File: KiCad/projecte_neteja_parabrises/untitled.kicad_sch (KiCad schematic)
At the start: 14 parts, among them J2 DE9_Pins, J3 DE9_Pins, SW1 CALEFACTOR, SW2 BOMBAS, SW5 SW_Rotary_1x5_MP, U1 TJA1049TK-3, U7 MAX232

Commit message: Error de nombres solucionado
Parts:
- renumbered U1 to U8, U7 to U9
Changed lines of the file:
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@@
 		(dnp no)
 		(fields_autoplaced yes)
-		(property "Reference" "U7"
+		(property "Reference" "U9"
 			(at 56.7533 31.75 0)
 			(effects
@@
 			(project "projecte_neteja_parabrises"
 				(path "/83fe8808-b70b-463e-9fcd-89556c9690a9/281f4b1b-fa83-45a0-8e9c-797a6b6648f6"
-					(reference "U7")
+					(reference "U9")
 					(unit 1)
 				)
@@
 		(dnp no)
 		(fields_autoplaced yes)
-		(property "Reference" "U1"
+		(property "Reference" "U8"
 			(at 209.7883 54.61 0)
 			(effects
@@
 			(project "projecte_neteja_parabrises"
 				(path "/83fe8808-b70b-463e-9fcd-89556c9690a9/281f4b1b-fa83-45a0-8e9c-797a6b6648f6"
-					(reference "U1")
-					(unit 1)
-				)
+					(reference "U8")
+					(unit 1)
+				)

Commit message: huellas
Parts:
- C18, C19, C5, C6, C7, C8, C9: footprint (none) -> Capacitor_SMD:C_0805_2012Metric
- U9: footprint (none) -> Package_SO:JEITA_SOIC-16_3.9x9.9mm_P1.27mm
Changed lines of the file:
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@@
 			)
 		)
-		(property "Footprint" ""
+		(property "Footprint" "Capacitor_SMD:C_0805_2012Metric"
 			(at 78.105 53.0352 0)
 			(effects
@@
 			)
 		)
-		(property "Footprint" ""
+		(property "Footprint" "Capacitor_SMD:C_0805_2012Metric"
 			(at 230.2002 68.58 0)
 			(effects
@@
 			)
 		)
-		(property "Footprint" ""
+		(property "Footprint" "Package_SO:JEITA_SOIC-16_3.9x9.9mm_P1.27mm"
 			(at 55.88 88.9 0)
 			(effects
@@
 			)
 		)
-		(property "Footprint" ""
+		(property "Footprint" "Capacitor_SMD:C_0805_2012Metric"
 			(at 78.4352 46.99 0)
 			(effects
@@
 			)
 		)
-		(property "Footprint" ""
+		(property "Footprint" "Capacitor_SMD:C_0805_2012Metric"
 			(at 30.1752 46.99 0)
 			(effects
@@
 			)
 		)
-		(property "Footprint" ""
+		(property "Footprint" "Capacitor_SMD:C_0805_2012Metric"
 			(at 79.375 60.6552 0)
 			(effects
@@
 			)
 		)
-		(property "Footprint" ""
+		(property "Footprint" "Capacitor_SMD:C_0805_2012Metric"
 			(at 230.2002 76.2 0)
 			(effects
@@
 			)
 		)
-		(property "Footprint" ""
+		(property "Footprint" "Capacitor_SMD:C_0805_2012Metric"
 			(at 54.61 25.7048 0)
 			(effects

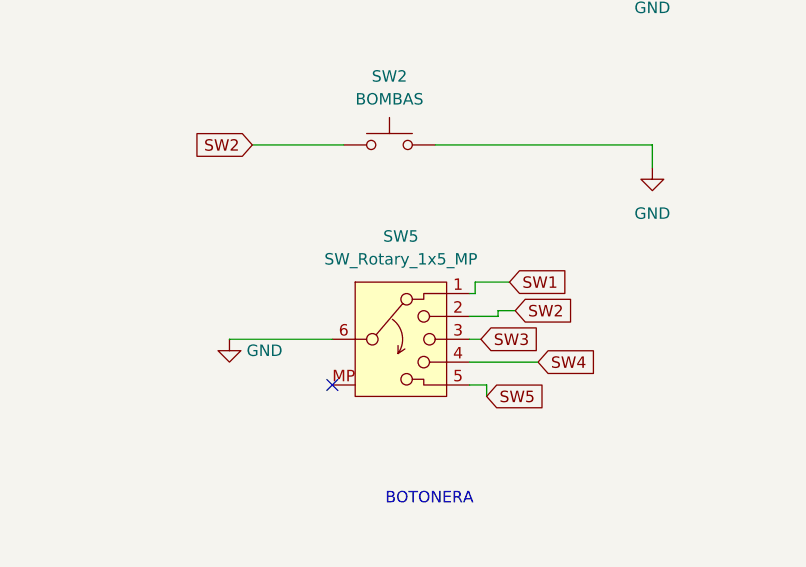
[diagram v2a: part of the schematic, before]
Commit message: Actualización huellas
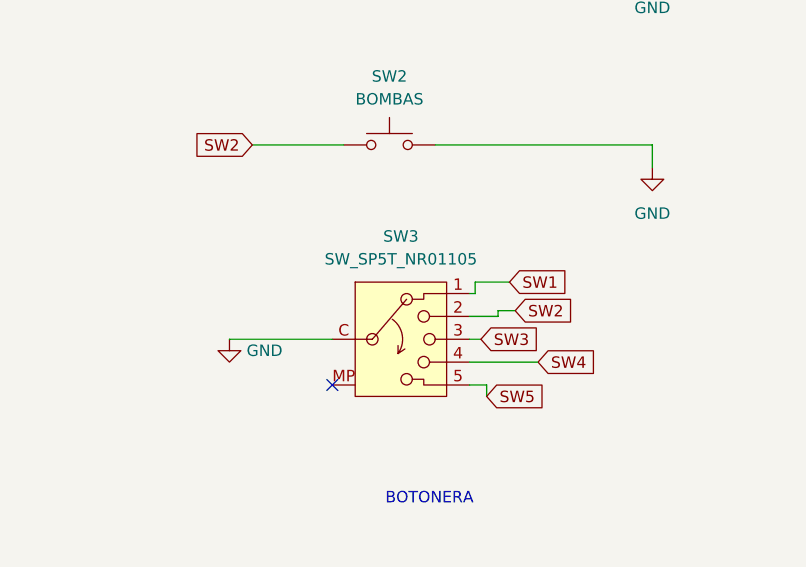
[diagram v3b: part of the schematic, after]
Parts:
- removed SW5: SW_Rotary_1x5_MP, symbol Switch:SW_Rotary_1x5_MP
- added SW3: SW_SP5T_NR01105, Button_Switch_THT:SW_NKK_NR01, symbol Switch:SW_SP5T_NR01105
- J2, J3: footprint (none) -> Connector_Dsub:DSUB-9_Pins_Horizontal_P2.77x2.84mm_EdgePinOffset4.94mm_Housed_MountingHolesOffset4.94mm
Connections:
- net GND: now also SW3.C (Common)
- net SW1: now also SW3.1
- net SW2: now also SW3.2
- net SW3: now also SW3.3
- net SW4: now also SW3.4
- net SW5: now also SW3.5
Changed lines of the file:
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@@
 			)
 		)
-		(property "Footprint" ""
+		(property "Footprint" "Connector_Dsub:DSUB-9_Pins_Horizontal_P2.77x2.84mm_EdgePinOffset4.94mm_Housed_MountingHolesOffset4.94mm"
 			(at 254.635 66.675 0)
 			(effects
@@
 			)
 		)
-		(property "Footprint" ""
+		(property "Footprint" "Connector_Dsub:DSUB-9_Pins_Horizontal_P2.77x2.84mm_EdgePinOffset4.94mm_Housed_MountingHolesOffset4.94mm"
 			(at 111.125 71.12 0)
 			(effects
@@
 	)
 	(symbol
+		(lib_id "Switch:SW_SP5T_NR01105")
+		(at 54.61 173.99 0)
+		(unit 1)
+		(exclude_from_sim no)
+		(in_bom yes)
+		(on_board yes)
+		(dnp no)
+		(fields_autoplaced yes)
+		(property "Reference" "SW3"
+			(at 54.61 162.56 0)
+			(effects
+				(font
+					(size 1.27 1.27)
+				)
+			)
+		)
+		(property "Value" "SW_SP5T_NR01105"
+			(at 54.61 165.1 0)
+			(effects
+				(font
+					(size 1.27 1.27)
+				)
+			)
+		)
+		(property "Footprint" "Button_Switch_THT:SW_NKK_NR01"
+			(at 54.61 184.15 0)
+			(effects
+				(font
+					(size 1.27 1.27)
+				)
+				(hide yes)
+			)
+		)
+		(property "Datasheet" "https://www.nkkswitches.com/pdf/NR01%20Rotaries.pdf"
+			(at 54.61 186.69 0)
+			(effects
+				(font
+					(size 1.27 1.27)
+				)
+				(hide yes)
+			)
+		)
+		(property "Description" "NKK Switches NR01 Series rotary SP5T switch"
+			(at 54.61 173.99 0)
+			(effects
+				(font
+					(size 1.27 1.27)
+				)
+				(hide yes)
+			)
+		)
+		(pin "C"
+		)
+		(pin "1"
+		)
+		(pin "2"
+		)
+		(pin "MP"
+		)
+		(pin "4"
+		)
+		(pin "3"
+		)
+		(pin "5"
+		)
+		(instances
+			(project ""
+				(path "/83fe8808-b70b-463e-9fcd-89556c9690a9/281f4b1b-fa83-45a0-8e9c-797a6b6648f6"
+					(reference "SW3")
+					(unit 1)
+				)
+			)
+		)
+	)
+	(symbol
 		(lib_id "power:GND")
 		(at 85.725 52.07 0)
@@
 					(unit 1)
 				)
-			)
-		)
-	)
-	(symbol
-		(lib_id "Switch:SW_Rotary_1x5_MP")
-		(at 54.61 173.99 0)
-		(unit 1)
-		(exclude_from_sim no)
-		(in_bom yes)
-		(on_board yes)
-		(dnp no)
-		(fields_autoplaced yes)
-		(property "Reference" "SW5"
-			(at 54.61 162.56 0)
-			(effects
-				(font
-					(size 1.27 1.27)
-				)
-			)
-		)
-		(property "Value" "SW_Rotary_1x5_MP"
-			(at 54.61 165.1 0)
-			(effects
-				(font
-					(size 1.27 1.27)
-				)
-			)
-		)
-		(property "Footprint" ""
-			(at 54.61 184.15 0)
-			(effects
-				(font
-					(size 1.27 1.27)
-				)
-				(hide yes)
-			)
-		)
-		(property "Datasheet" "~"
-			(at 54.61 186.69 0)
-			(effects
-				(font
-					(size 1.27 1.27)
-				)
-				(hide yes)
-			)
-		)
-		(property "Description" "Rotary switch 1x5, SP5T with mount point"
-			(at 54.61 173.99 0)
-			(effects
-				(font
-					(size 1.27 1.27)
-				)
-				(hide yes)
-			)
-		)
-		(pin "1"
-		)
-		(pin "2"
-		)
-		(pin "MP"
-		)
-		(pin "3"
-		)
-		(pin "4"
-		)
-		(pin "6"
-		)
-		(pin "5"
-		)
-		(instances
-			(project "projecte_neteja_parabrises"
-				(path "/83fe8808-b70b-463e-9fcd-89556c9690a9/281f4b1b-fa83-45a0-8e9c-797a6b6648f6"
-					(reference "SW5")
-					(unit 1)
-				)

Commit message: botonera
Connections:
- net SW1: no longer SW1.1
- net SW2: no longer SW2.1
- new net SWB: SW2.1
- new net SWC: SW1.1
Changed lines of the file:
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@@
 		)
 	)
-	(global_label "SW2"
+	(global_label "SWB"
 		(shape input)
 		(at 38.1 152.4 180)
@@
 		)
 		(property "Intersheetrefs" "${INTERSHEET_REFS}"
-			(at 31.2444 152.4 0)
+			(at 31.1839 152.4 0)
 			(effects
 				(font
@@
 		)
 	)
-	(global_label "SW1"
+	(global_label "SWC"
 		(shape input)
 		(at 38.1 129.54 180)
@@
 		)
 		(property "Intersheetrefs" "${INTERSHEET_REFS}"
-			(at 31.2444 129.54 0)
+			(at 31.1839 129.54 0)
 			(effects
 				(font

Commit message: Placa definitiva
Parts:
- J2, J3: footprint Connector_Dsub:DSUB-9_Pins_Horizontal_P2.77x2.84mm_EdgePinOffset4.94mm_Housed_MountingHolesOffset4.94mm -> Connector_Dsub:DSUB-9_Pins_Vertical_P2.77x2.84mm
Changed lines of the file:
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@@
-	(wire
-		(pts
-			(xy 65.405 170.815) (xy 65.405 171.45)
-		)
-		(stroke
-			(width 0)
-			(type default)
-		)
-	)
 	(wire
 		(pts
@@
 	(wire
 		(pts
-			(xy 62.865 167.64) (xy 62.865 168.91)
-		)
-		(stroke
-			(width 0)
-			(type default)
-		)
-	)
-	(wire
-		(pts
 			(xy 76.835 74.93) (xy 74.93 74.93)
 		)
@@
 	(wire
 		(pts
-			(xy 64.135 179.07) (xy 62.23 179.07)
+			(xy 65.405 179.07) (xy 62.23 179.07)
 		)
 		(stroke
@@
 	(wire
 		(pts
-			(xy 62.865 168.91) (xy 62.23 168.91)
+			(xy 62.23 168.91) (xy 69.215 168.91)
 		)
 		(stroke
@@
 	(wire
 		(pts
-			(xy 64.135 180.34) (xy 64.135 179.07)
-		)
-		(stroke
-			(width 0)
-			(type default)
-		)
-	)
-	(wire
-		(pts
-			(xy 67.31 170.815) (xy 65.405 170.815)
-		)
-		(stroke
-			(width 0)
-			(type default)
-		)
-	)
-	(wire
-		(pts
 			(xy 229.235 68.58) (xy 238.125 68.58)
 		)
@@
 	(wire
 		(pts
-			(xy 62.865 167.64) (xy 66.675 167.64)
-		)
-		(stroke
-			(width 0)
-			(type default)
-		)
-	)
-	(wire
-		(pts
 			(xy 220.345 60.96) (xy 220.345 64.77)
 		)
@@
 	(wire
 		(pts
-			(xy 69.85 176.53) (xy 62.23 176.53)
+			(xy 76.2 176.53) (xy 62.23 176.53)
 		)
 		(stroke
@@
 	(wire
 		(pts
-			(xy 65.405 171.45) (xy 62.23 171.45)
+			(xy 62.23 171.45) (xy 75.565 171.45)
 		)
 		(stroke
@@
 	(global_label "SW2"
 		(shape input)
-		(at 67.31 170.815 0)
+		(at 75.565 171.45 0)
 		(fields_autoplaced yes)
 		(effects
@@
 		)
 		(property "Intersheetrefs" "${INTERSHEET_REFS}"
-			(at 74.1656 170.815 0)
+			(at 82.4206 171.45 0)
 			(effects
 				(font
@@
 	(global_label "SW5"
 		(shape input)
-		(at 64.135 180.34 0)
+		(at 65.405 179.07 0)
 		(fields_autoplaced yes)
 		(effects
@@
 		)
 		(property "Intersheetrefs" "${INTERSHEET_REFS}"
-			(at 70.9906 180.34 0)
+			(at 72.2606 179.07 0)
 			(effects
 				(font
@@
 	(global_label "SW1"
 		(shape input)
-		(at 66.675 167.64 0)
+		(at 69.215 168.91 0)
 		(fields_autoplaced yes)
 		(effects
@@
 		)
 		(property "Intersheetrefs" "${INTERSHEET_REFS}"
-			(at 73.5306 167.64 0)
+			(at 76.0706 168.91 0)
 			(effects
 				(font
@@
 	(global_label "SW4"
 		(shape input)
-		(at 69.85 176.53 0)
+		(at 76.2 176.53 0)
 		(fields_autoplaced yes)
 		(effects
@@
 		)
 		(property "Intersheetrefs" "${INTERSHEET_REFS}"
-			(at 76.7056 176.53 0)
+			(at 83.0556 176.53 0)
 			(effects
 				(font
@@
 			)
 		)
-		(property "Footprint" "Connector_Dsub:DSUB-9_Pins_Horizontal_P2.77x2.84mm_EdgePinOffset4.94mm_Housed_MountingHolesOffset4.94mm"
+		(property "Footprint" "Connector_Dsub:DSUB-9_Pins_Vertical_P2.77x2.84mm"
 			(at 254.635 66.675 0)
 			(effects
@@
 			)
 		)
-		(property "Footprint" "Connector_Dsub:DSUB-9_Pins_Horizontal_P2.77x2.84mm_EdgePinOffset4.94mm_Housed_MountingHolesOffset4.94mm"
+		(property "Footprint" "Connector_Dsub:DSUB-9_Pins_Vertical_P2.77x2.84mm"
 			(at 111.125 71.12 0)
 			(effects

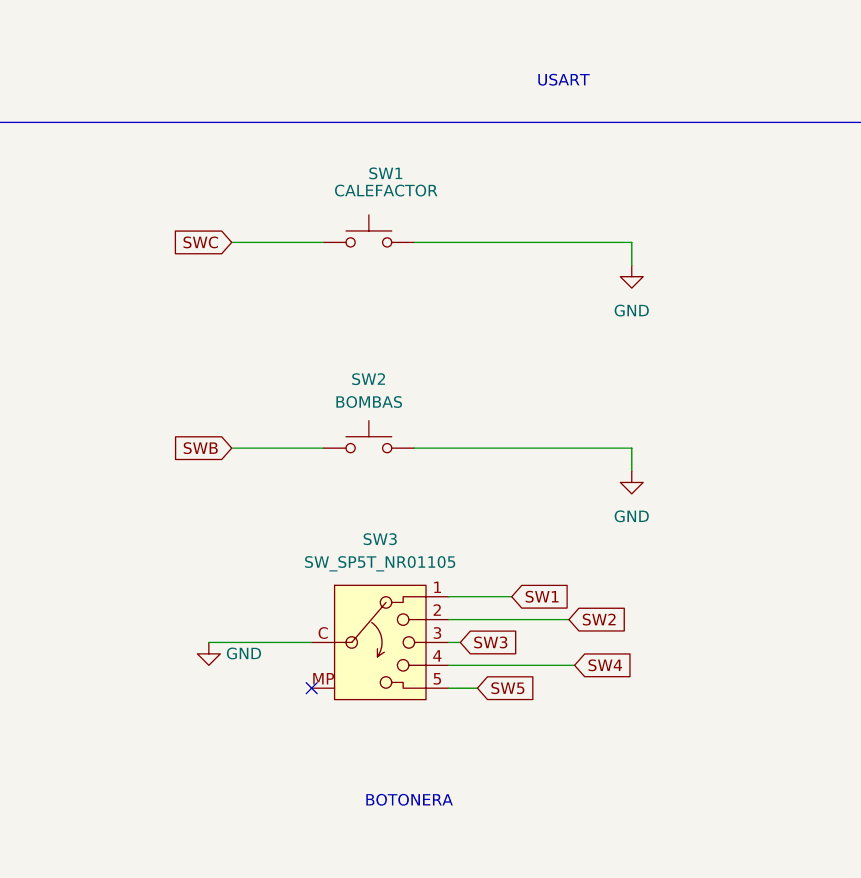
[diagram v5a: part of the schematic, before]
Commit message: millora botonera
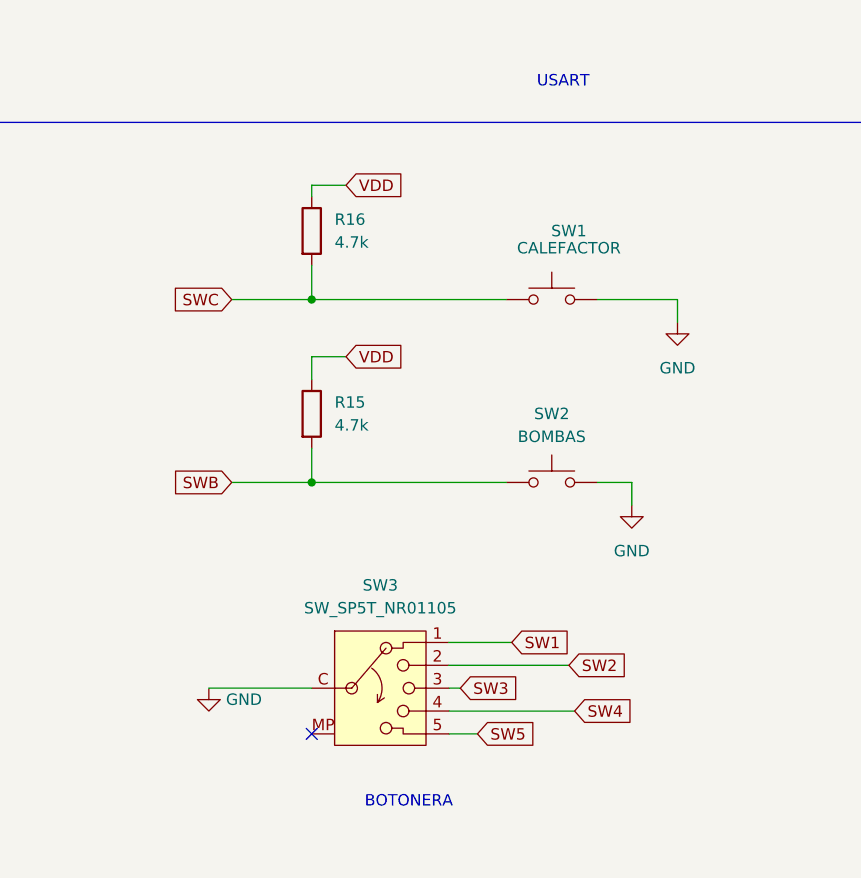
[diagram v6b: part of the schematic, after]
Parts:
- added R15, R16: 4.7k, Resistor_SMD:R_0603_1608Metric_Pad0.98x0.95mm_HandSolder, symbol Device:R
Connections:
- net SWB: now also R15.2
- net SWC: now also R16.2
- net VDD: now also R15.1, R16.1
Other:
- moved on the sheet: SW1, SW2, SW3
